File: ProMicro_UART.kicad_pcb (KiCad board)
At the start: 2 copper layers, 17.8 x 33 mm, 55 parts, among them J2 Conn_01x06, J3 USB_B_Mini, U1 FT232H, U2 93CxxB, U3 AZ1117-3.3, U4 FT232RL, Y1 12Mhz

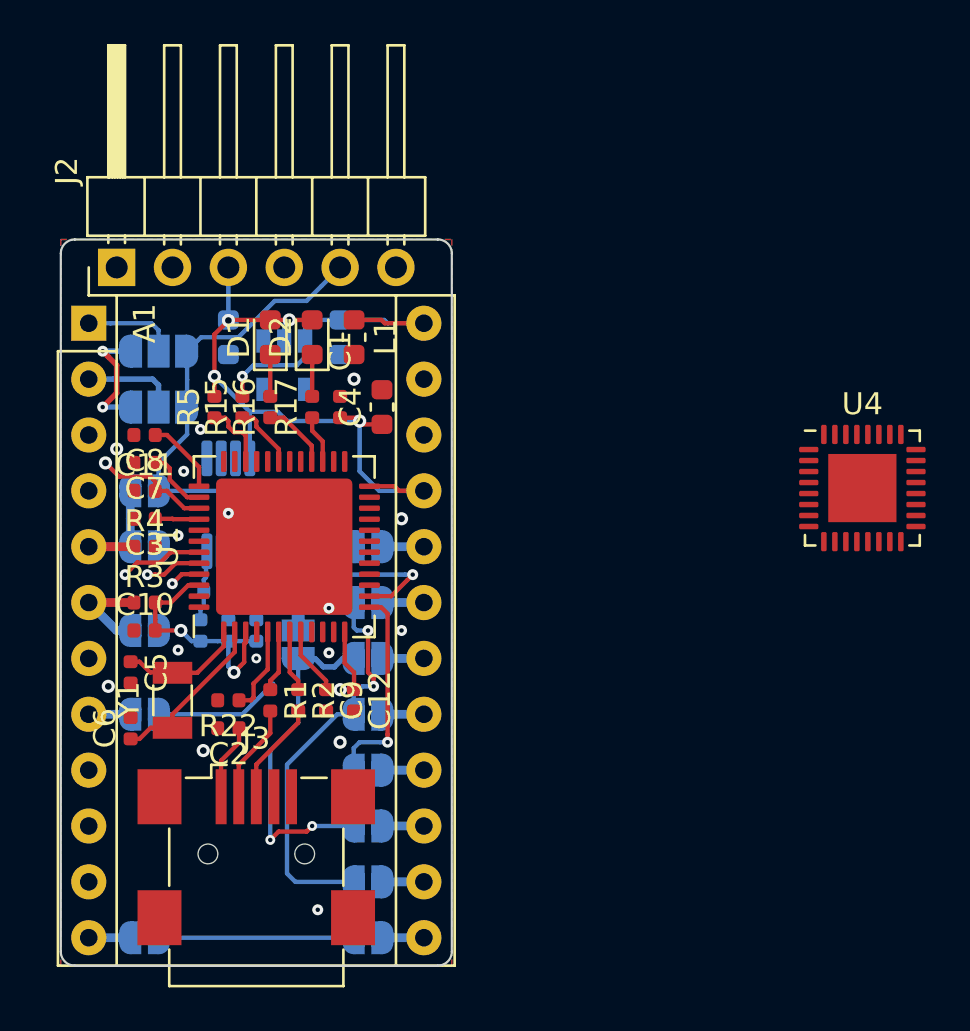
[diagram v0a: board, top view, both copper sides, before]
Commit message: fully routed
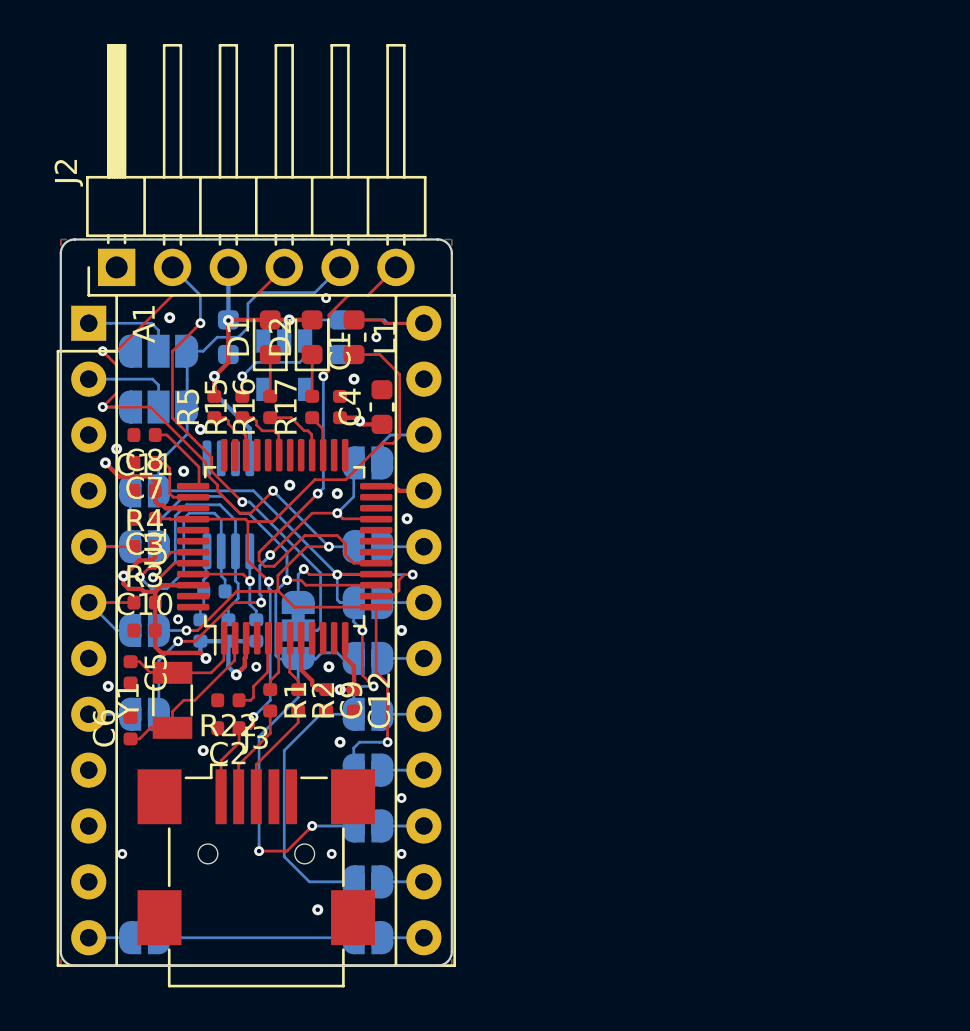
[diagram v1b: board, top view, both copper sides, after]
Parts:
- removed U4: FT232RL, Package_DFN_QFN:QFN-32-1EP_5x5mm_P0.5mm_EP3.1x3.1mm
- added JP17: Jumper_NO_Small, Jumper:SolderJumper-2_P1.3mm_Open_RoundedPad1.0x1.5mm, B.Cu at (114.3, 82.5)
- U1: footprint Package_DFN_QFN:QFN-48-1EP_8x8mm_P0.5mm_EP6.2x6.2mm -> Package_QFP:LQFP-48_7x7mm_P0.5mm
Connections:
- A1 pad 22: ACBUS0 -> Reset
- J2 pad 5: ADBUS1 -> ADBUS3
- JP10 pad 1: ADBUS1 -> ADBUS3
- JP11 pad 3: ADBUS1 -> ADBUS3
- JP13 pad 1: ADBUS1 -> ADBUS3
- JP2 pad 1: ADBUS1 -> ADBUS3
- JP7 pad 1: ADBUS1 -> ADBUS3
- U1 pad 14: ADBUS1 -> ADBUS3
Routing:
- net ADBUS0: track 15.0 -> 54.2 mm, vias 3 -> 6
- net ADBUS3: track 32.8 -> 68.7 mm, vias 2 -> 5
- net ADBUS1: track 31.8 -> 0.00 mm, vias 1 -> 0
- net Net-(C2-Pad1): track 5.43 -> 32.4 mm, vias 0 -> 2
- net ADBUS4: track 0.00 -> 23.3 mm, vias 0 -> 2
- net Net-(J2-Pad2): track 0.00 -> 21.5 mm, vias 0 -> 2
- net ADBUS2: track 15.7 -> 35.7 mm, vias 2 -> 3
- net ACBUS0: track 5.77 -> 18.9 mm, vias 0 -> 4
- net /EECLK: track 5.94 -> 13.7 mm
- net /EEDAT: track 5.68 -> 13.4 mm
- net +3V3: track 55.2 -> 51.5 mm, vias 8 -> 9
- net Reset: track 0.00 -> 2.95 mm
- net /EECS: track 4.63 -> 5.95 mm
- net GND: vias 14 -> 22
- net (no net): vias 2 -> 0
- added copper zone on In1.Cu, net +3V3
- added copper zone on In2.Cu, net GND
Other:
- copper layers 2 -> 4
- net class Default: clearance 0.2 -> 0.125; trace_width 0.25 -> 0.125; via_dia 0.5 -> 0.45
- net class Power: trace_width 0.4 -> 0.2; via_dia 0.6 -> 0.5; via_drill 0.3 -> 0.2
- net class small removed
- net class tiny removed
- rule trace_clearance: 0.2 -> 0.125
- board text added: "github.com/nerdyscout/ProMicro_UART"
- board text added: "v1.0"
- board text removed: "Revision: %R"
- board text removed: "github.com/nerdyscout/ProMicro_Serial"

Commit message: rotated breakout pins
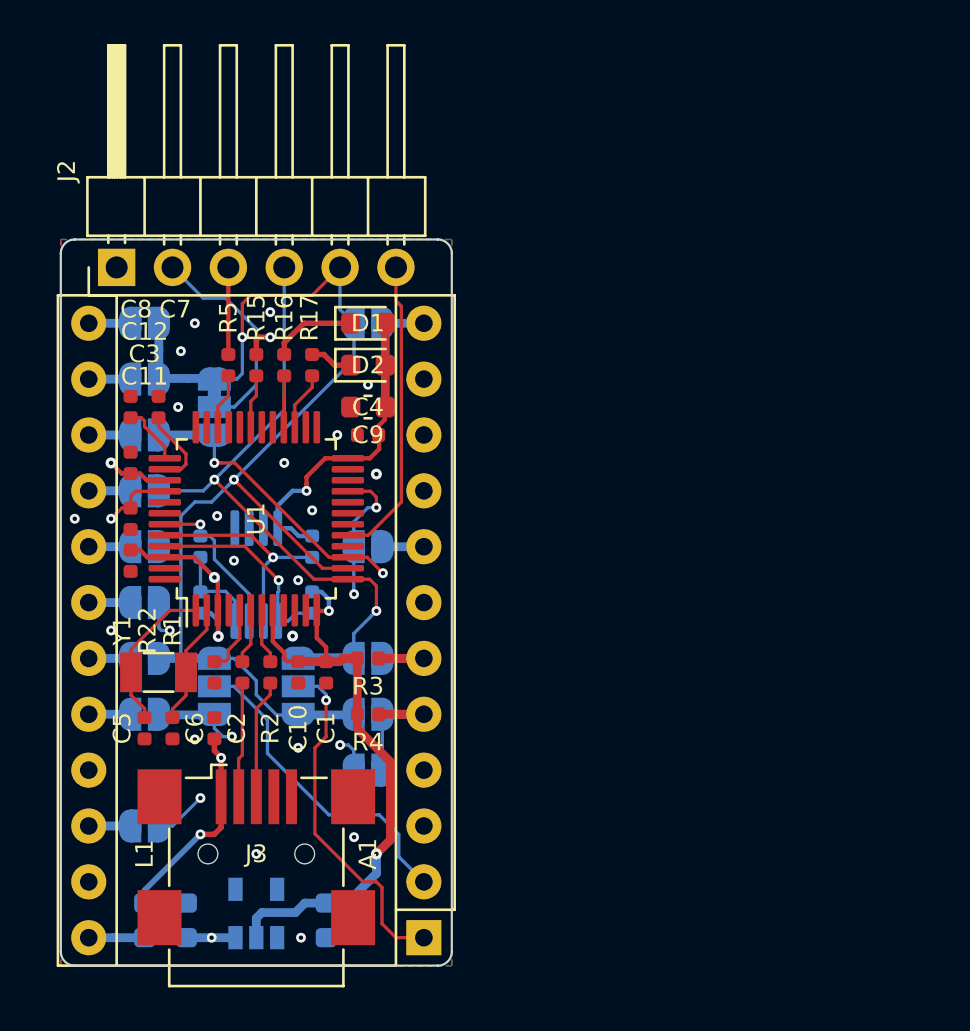
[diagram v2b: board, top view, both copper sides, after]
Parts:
- L1: moved to B.Cu
- moved A1 31.8 mm to (116.8, 104.1), turned to 180 degrees
- moved JP4 29.7 mm to (114.3, 76.2), turned to 0 degrees
- moved JP5 29.7 mm to (104.1, 76.2), turned to 180 degrees
- moved L1 28.2 mm to (104.1, 103.4), turned to 90 degrees
- moved C13 27.4 mm to (106.0, 103.4), turned to 90 degrees
- moved C14 26.9 mm to (112.4, 103.4)
- moved JP2 25.0 mm to (104.1, 78.7), turned to 180 degrees
- moved U3 25.0 mm to (109.2, 103.0), turned to 90 degrees
- moved LOGO1 20.6 mm to (109.2, 97.0), turned to 180 degrees
- moved JP3 20.5 mm to (104.1, 81.3), turned to 180 degrees
- moved JP17 19.4 mm to (104.1, 99.1), turned to 180 degrees
- moved JP10 16.5 mm to (111.1, 92.7), turned to 90 degrees
- moved JP1 16.3 mm to (104.1, 83.8), turned to 180 degrees
- moved C12 14.8 mm to (103.5, 82.5), turned to 90 degrees
- moved JP13 14.4 mm to (114.3, 94.0), turned to 0 degrees
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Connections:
- J2 pad 5: ADBUS3 -> ADBUS1
- JP10 pad 1: ADBUS3 -> ADBUS1
- JP11 pad 3: ADBUS3 -> ADBUS1
- JP13 pad 1: ADBUS3 -> ADBUS1
- JP16 pad 1: ADBUS3 -> ADBUS1
- JP2 pad 1: ADBUS3 -> ADBUS1
- JP4 pad 1: ADBUS3 -> ADBUS1
- JP5 pad 1: ADBUS3 -> ADBUS1
- JP7 pad 1: ADBUS3 -> ADBUS1
- JP9 pad 1: ADBUS3 -> ADBUS1
- U1 pad 14: ADBUS3 -> ADBUS1
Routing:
- net ADBUS3: track 68.7 -> 0.00 mm, vias 5 -> 0
- net ADBUS1: track 0.00 -> 54.6 mm, vias 0 -> 2
- net +5V: track 14.4 -> 46.8 mm, vias 1 -> 2
- net ADBUS0: track 54.2 -> 42.3 mm, vias 6 -> 3
- net Net-(J2-Pad2): track 21.5 -> 9.84 mm, vias 2 -> 0
- net D1: track 4.26 -> 15.8 mm, vias 0 -> 1
- net D0: track 4.29 -> 14.7 mm
- net ADBUS4: track 23.3 -> 13.8 mm, vias 2 -> 0
- net Net-(C2-Pad1): track 32.4 -> 25.6 mm, vias 2 -> 3
- net +3V3: track 51.5 -> 58.2 mm, vias 9 -> 6
- net /EEDAT: track 13.4 -> 7.17 mm
- net /EECLK: track 13.7 -> 10.2 mm
- net /EECS: track 5.95 -> 9.41 mm
- net ACBUS0: track 18.9 -> 21.6 mm, vias 4 -> 3
- net Net-(C6-Pad1): track 7.94 -> 5.52 mm
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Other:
- net class Default: clearance 0.125 -> 0.15; trace_width 0.125 -> 0.15
- rule trace_clearance: 0.125 -> 0.15
- board text added: "ProMicro_UART"
- board text removed: "github.com/nerdyscout/ProMicro_UART"

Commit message: new docs
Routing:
- net Net-(C2-Pad1): track 25.6 -> 27.2 mm
- net GND: vias 20 -> 22
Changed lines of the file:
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@@
     (thickness 0.8)
     (drawings 12)
-    (tracks 373)
+    (tracks 377)
     (zones 0)
     (modules 55)
@@
   )
   (layers
-    (0 F.Cu mixed hide)
-    (1 In1.Cu signal hide)
-    (2 In2.Cu signal hide)
-    (31 B.Cu mixed hide)
-    (32 B.Adhes user hide)
-    (33 F.Adhes user hide)
+    (0 F.Cu mixed)
+    (1 In1.Cu signal)
+    (2 In2.Cu signal)
+    (31 B.Cu mixed)
+    (32 B.Adhes user)
+    (33 F.Adhes user)
     (34 B.Paste user)
-    (35 F.Paste user hide)
+    (35 F.Paste user)
     (36 B.SilkS user)
-    (37 F.SilkS user hide)
+    (37 F.SilkS user)
     (38 B.Mask user)
-    (39 F.Mask user hide)
+    (39 F.Mask user)
     (40 Dwgs.User user hide)
     (41 Cmts.User user hide)
@@
   )
   (setup
-    (last_trace_width 0.25)
+    (last_trace_width 0.15)
     (user_trace_width 0.1)
     (user_trace_width 0.2)
@@
     (tags capacitor)
     (attr smd)
-    (fp_text reference C9 (at 0 0) (layer F.SilkS)
+    (fp_text reference C9 (at -0.762 -1.397 90) (layer F.SilkS)
       (effects (font (size 0.8 0.8) (thickness 0.2)))
     )
@@
     (tags capacitor)
     (attr smd)
-    (fp_text reference C4 (at 0 0) (layer F.SilkS)
+    (fp_text reference C4 (at 2.54 0.508) (layer F.SilkS)
       (effects (font (size 0.8 0.8) (thickness 0.2)))
     )
@@
   (gr_line (start 118.11 73.025) (end 118.11 104.775) (layer Edge.Cuts) (width 0.1))
   (gr_line (start 100.965 72.39) (end 117.475 72.39) (layer Edge.Cuts) (width 0.1))
-  (via (at 110.871 90.424) (size 0.5) (drill 0.2) (layers F.Cu B.Cu) (net 1))
+  (via (at 110.871 90.424) (size 0.45) (drill 0.2) (layers F.Cu B.Cu) (net 1))
   (via (at 111.252 104.14) (size 0.45) (drill 0.2) (layers F.Cu B.Cu) (net 1))
   (via (at 106.426 95.123) (size 0.45) (drill 0.2) (layers F.Cu B.Cu) (net 1))
@@
   (via (at 105.791 77.47) (size 0.45) (drill 0.2) (layers F.Cu B.Cu) (net 1))
   (via (at 111.125 87.884) (size 0.45) (drill 0.2) (layers F.Cu B.Cu) (net 1))
-  (via (at 102.616 90.17) (size 0.45) (drill 0.2) (layers F.Cu B.Cu) (net 1))
   (via (at 107.442 84.963) (size 0.45) (drill 0.2) (layers F.Cu B.Cu) (net 1))
   (via (at 111.76 84.709) (size 0.45) (drill 0.2) (layers F.Cu B.Cu) (net 1))
@@
   (via (at 109.22 100.33) (size 0.45) (drill 0.2) (layers F.Cu B.Cu) (net 1))
   (via (at 113.665 99.568) (size 0.45) (drill 0.2) (layers F.Cu B.Cu) (net 1))
+  (via (at 116.205 102.87) (size 0.45) (drill 0.2) (layers F.Cu B.Cu) (net 1))
+  (via (at 102.616 90.17) (size 0.45) (drill 0.2) (layers F.Cu B.Cu) (net 1))
+  (via (at 104.775 92.71) (size 0.45) (drill 0.2) (layers F.Cu B.Cu) (net 1))
   (segment (start 110.617 91.567) (end 111.125 91.567) (width 0.2) (layer F.Cu) (net 2))
   (segment (start 110.49 91.186) (end 110.49 91.44) (width 0.2) (layer F.Cu) (net 2))
@@
   (segment (start 103.505 84.605) (end 103.101 84.605) (width 0.15) (layer F.Cu) (net 4))
   (segment (start 103.101 84.605) (end 102.616 85.09) (width 0.15) (layer F.Cu) (net 4))
-  (segment (start 104.14 102.565) (end 104.14 102.1275) (width 0.25) (layer B.Cu) (net 4))
-  (segment (start 107.62 99.13) (end 107.309 99.441) (width 0.25) (layer F.Cu) (net 4))
-  (segment (start 107.62 97.73) (end 107.62 99.13) (width 0.25) (layer F.Cu) (net 4))
-  (segment (start 107.309 99.441) (end 106.68 99.441) (width 0.25) (layer F.Cu) (net 4))
-  (segment (start 104.14 101.981) (end 106.68 99.441) (width 0.25) (layer B.Cu) (net 4))
-  (via (at 106.68 99.441) (size 0.45) (drill 0.2) (layers F.Cu B.Cu) (net 4))
-  (segment (start 104.14 102.1275) (end 104.14 101.981) (width 0.25) (layer B.Cu) (net 4))
   (via (at 107.62 95.961) (size 0.45) (drill 0.2) (layers F.Cu B.Cu) (net 4))
-  (segment (start 103.124 85.598) (end 102.616 85.09) (width 0.15) (layer In1.Cu) (net 4))
+  (via (at 107.95 100.33) (size 0.45) (drill 0.2) (layers F.Cu B.Cu) (net 4))
+  (segment (start 107.95 99.695) (end 107.95 100.33) (width 0.25) (layer F.Cu) (net 4))
+  (segment (start 107.62 97.73) (end 107.62 99.365) (width 0.25) (layer F.Cu) (net 4))
+  (segment (start 107.62 99.365) (end 107.95 99.695) (width 0.25) (layer F.Cu) (net 4))
+  (segment (start 107.95 100.648198) (end 107.95 100.33) (width 0.25) (layer B.Cu) (net 4))
+  (segment (start 107.543197 101.055001) (end 107.95 100.648198) (width 0.25) (layer B.Cu) (net 4))
+  (segment (start 104.631249 101.055001) (end 107.543197 101.055001) (width 0.25) (layer B.Cu) (net 4))
+  (segment (start 104.14 102.565) (end 104.14 101.54625) (width 0.25) (layer B.Cu) (net 4))
+  (segment (start 104.14 101.54625) (end 104.631249 101.055001) (width 0.25) (layer B.Cu) (net 4))
+  (segment (start 107.62 94.666) (end 103.505 90.551) (width 0.15) (layer In1.Cu) (net 4))
+  (segment (start 103.505 90.551) (end 103.505 85.979) (width 0.15) (layer In1.Cu) (net 4))
   (segment (start 107.62 95.961) (end 107.62 94.666) (width 0.15) (layer In1.Cu) (net 4))
-  (segment (start 103.124 90.17) (end 103.124 85.598) (width 0.15) (layer In1.Cu) (net 4))
-  (segment (start 107.62 94.666) (end 103.124 90.17) (width 0.15) (layer In1.Cu) (net 4))
+  (segment (start 103.505 85.979) (end 102.616 85.09) (width 0.15) (layer In1.Cu) (net 4))
   (segment (start 104.14 94.13) (end 104.14 93.726) (width 0.15) (layer F.Cu) (net 5))
   (segment (start 103.525 93.111) (end 103.525 92.075) (width 0.15) (layer F.Cu) (net 5))
@@
   (segment (start 109.22 77.62) (end 109.22 76.962) (width 0.25) (layer F.Cu) (net 18))
   (segment (start 109.22 76.962) (end 109.347 76.835) (width 0.25) (layer F.Cu) (net 18))
+  (segment (start 114.808 104.902) (end 115.57 104.14) (width 0.4) (layer In1.Cu) (net 18))
+  (segment (start 115.57 104.14) (end 115.57 82.55) (width 0.4) (layer In1.Cu) (net 18))
+  (segment (start 107.188 104.14) (end 107.95 104.902) (width 0.4) (layer In1.Cu) (net 18))
   (segment (start 115.57 82.55) (end 109.855 76.835) (width 0.4) (layer In1.Cu) (net 18))
-  (segment (start 115.57 104.394) (end 115.57 82.55) (width 0.4) (layer In1.Cu) (net 18))
-  (segment (start 115.062 104.902) (end 115.57 104.394) (width 0.4) (layer In1.Cu) (net 18))
-  (segment (start 107.188 104.14) (end 107.95 104.902) (width 0.4) (layer In1.Cu) (net 18))
-  (segment (start 107.95 104.902) (end 115.062 104.902) (width 0.4) (layer In1.Cu) (net 18))
+  (segment (start 107.95 104.902) (end 114.808 104.902) (width 0.4) (layer In1.Cu) (net 18))
   (via (at 114.681 84.582) (size 0.45) (drill 0.2) (layers F.Cu B.Cu) (net 19))
   (segment (start 113.3825 83.84) (end 114.415599 83.84) (width 0.15) (layer F.Cu) (net 19))
@@
   (segment (start 112.025 92.71) (end 112.395 93.08) (width 0.15) (layer B.Cu) (net 33))
   (segment (start 111.125 92.71) (end 112.025 92.71) (width 0.15) (layer B.Cu) (net 33))
-  (segment (start 112.395 94.996) (end 112.395 93.345) (width 0.15) (layer F.Cu) (net 33))
-  (segment (start 111.887 95.504) (end 112.395 94.996) (width 0.15) (layer F.Cu) (net 33))
-  (segment (start 111.887 99.413999) (end 111.887 95.504) (width 0.15) (layer F.Cu) (net 33))
+  (segment (start 112.395 94.488) (end 112.395 93.345) (width 0.15) (layer F.Cu) (net 33))
   (segment (start 115.57 104.14) (end 114.935 103.505) (width 0.15) (layer F.Cu) (net 33))
   (segment (start 116.84 104.14) (end 115.57 104.14) (width 0.15) (layer F.Cu) (net 33))
+  (segment (start 111.887 99.413999) (end 111.887 94.996) (width 0.15) (layer F.Cu) (net 33))
+  (segment (start 114.073001 101.6) (end 111.887 99.413999) (width 0.15) (layer F.Cu) (net 33))
+  (segment (start 111.887 94.996) (end 112.395 94.488) (width 0.15) (layer F.Cu) (net 33))
   (segment (start 114.935 103.505) (end 114.935 101.854) (width 0.15) (layer F.Cu) (net 33))
   (segment (start 114.935 101.854) (end 114.681 101.6) (width 0.15) (layer F.Cu) (net 33))
   (segment (start 114.681 101.6) (end 114.073001 101.6) (width 0.15) (layer F.Cu) (net 33))
-  (segment (start 114.073001 101.6) (end 111.887 99.413999) (width 0.15) (layer F.Cu) (net 33))
   (segment (start 115.57 75.184) (end 115.57 73.66) (width 0.15) (layer F.Cu) (net 34))
   (segment (start 115.814999 75.428999) (end 115.57 75.184) (width 0.15) (layer F.Cu) (net 34))
@@
     (connect_pads (clearance 0.125))
     (min_thickness 0.254)
-    (fill yes (arc_segments 32) (thermal_gap 0.508) (thermal_bridge_width 0.508))
+    (fill yes (arc_segments 32) (thermal_gap 0.2) (thermal_bridge_width 0.3))
     (polygon
       (pts
@@
   (zone (net 1) (net_name GND) (layer In2.Cu) (hatch edge 0.508)
     (connect_pads (clearance 0.125))
-    (min_thickness 0.254)
-    (fill yes (arc_segments 32) (thermal_gap 0.508) (thermal_bridge_width 0.508))
+    (min_thickness 0.125)
+    (fill yes (arc_segments 32) (thermal_gap 0.2) (thermal_bridge_width 0.3))
     (polygon
       (pts

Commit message: a lot of docu
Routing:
- net Net-(C2-Pad1): track 27.2 -> 28.1 mm
- net GND: vias 22 -> 24
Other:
- board text added: "3V3"
- board text added: "5V"
- board text added: "CS0"
- board text added: "CS1"
- board text added: "GND"
- board text added: "I2C"
- board text added: "JTAG"
- board text added: "MISO"
- board text added: "MOSI"
- board text added: "RS485"
- board text added: "RXD"
- board text added: "SCK"
- board text added: "SCL"
- board text added: "SDA"
- board text added: "SPI"
- board text added: "TCK"
- board text added: "TDI"
- board text added: "TDO"
- board text added: "TMS"
- board text added: "TXD"
- board text added: "TXDEN"
- board text added: "UART"
- board text added: "v1.2"
- board text removed: "v1.0"
